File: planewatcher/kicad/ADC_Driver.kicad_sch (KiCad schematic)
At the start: 25 parts, among them U10 AD8138ARZ, U3 OPA2320

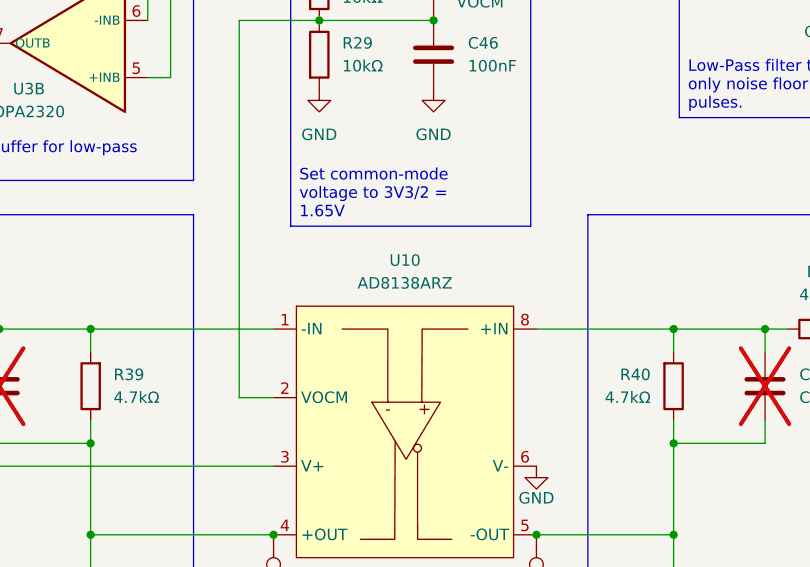
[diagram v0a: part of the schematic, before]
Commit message: Replace TADJ prototype trimmer with voltage divider
Voltage divider sets the ADL5513 TADJ pin to approximately 0.85 V for 1090 MHz operation
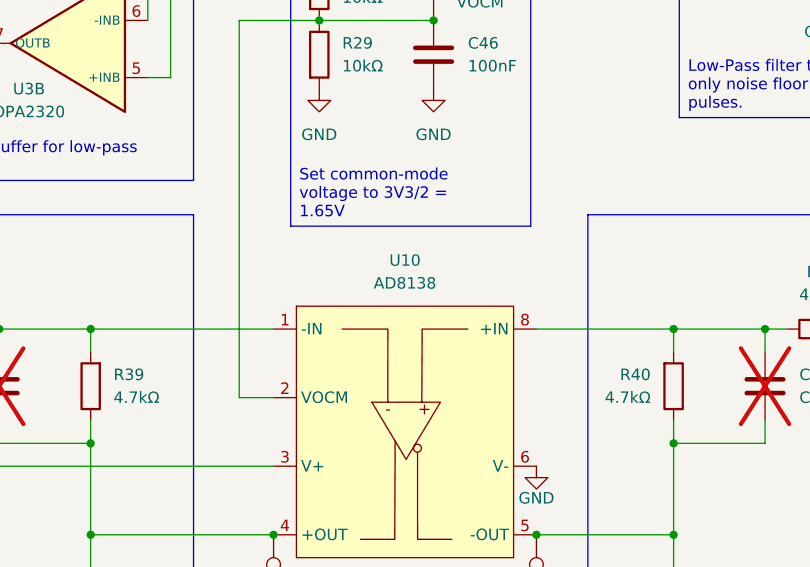
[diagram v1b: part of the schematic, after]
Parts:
- U10: value AD8138ARZ -> AD8138
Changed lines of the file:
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@@
 			)
 		)
-		(property "Value" "AD8138ARZ"
+		(property "Value" "AD8138"
 			(at 147.955 87.63 0)
 			(show_name no)

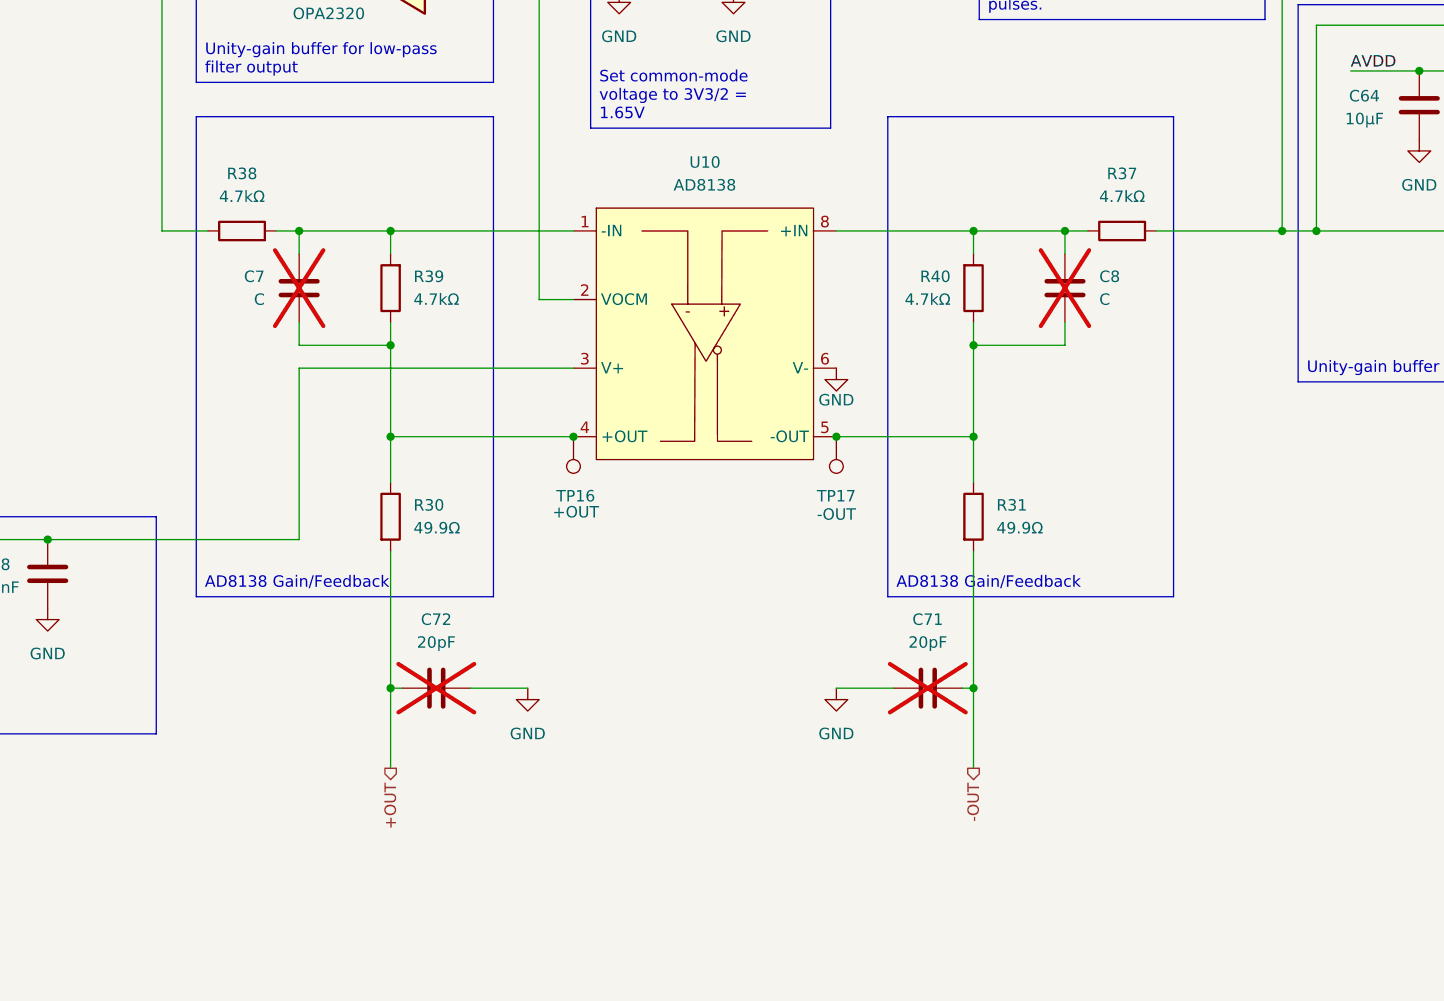
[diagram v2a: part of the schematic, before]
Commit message: Replace AD8138 gain/feedback resistors with resistor array
R37, R38, R39, R40 -> RN1.
Resolves: https://github.com/plane-watch/hardware/pull/5#issuecomment-4815513095
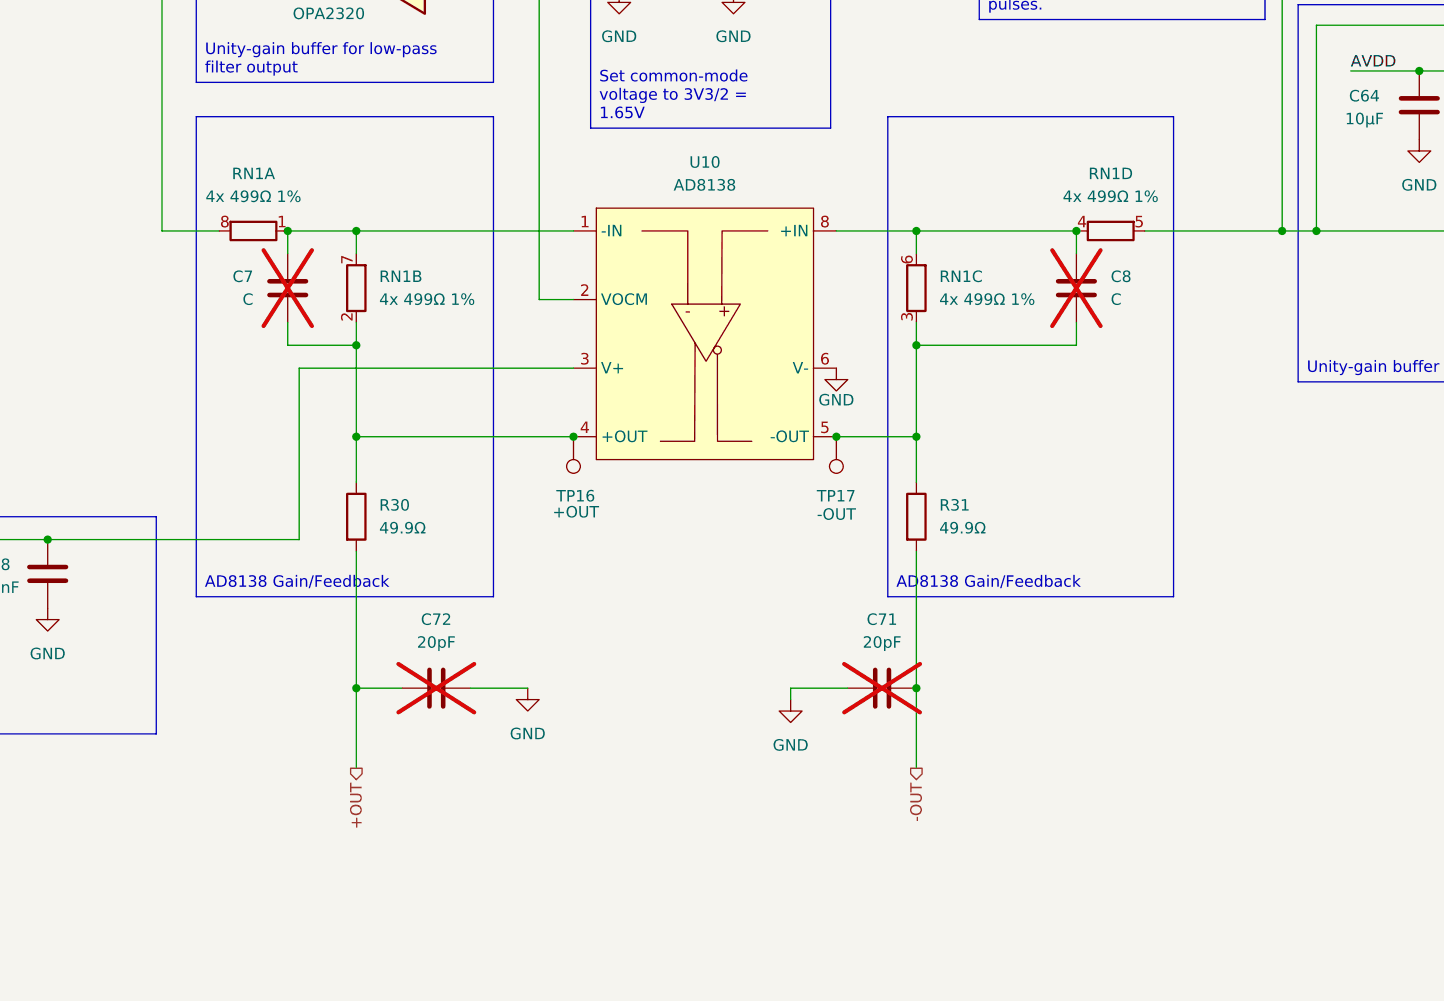
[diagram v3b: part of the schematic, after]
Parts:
- removed R37, R38, R39, R40: 4.7kΩ, Resistor_SMD:R_0402_1005Metric, symbol Device:R
- added RN1: 4x 499Ω 1%, Resistor_SMD:R_Array_Convex_4x0402, symbol Device:R_Pack04_Split
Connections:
- net at C7.2, R30.1, TP16.1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: now also RN1.2 (R2.1)
- net at C8.2, R31.1, TP17.1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: now also RN1.3 (R3.1)
- net at C8.1, U10.8 (+IN): now also RN1.4 (R4.1), RN1.6 (R3.2)
- net at C7.1, U10.1 (-IN): now also RN1.1 (R1.1), RN1.7 (R2.2)
- net at U3.6 (-INB), U3.7 (OUTB): now also RN1.8 (R1.2)
- net at R51.2, U3.1 (OUTA), U3.2 (-INA): now also RN1.5 (R4.2)
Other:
- moved on the sheet: C7, C71, C8, R30, R31

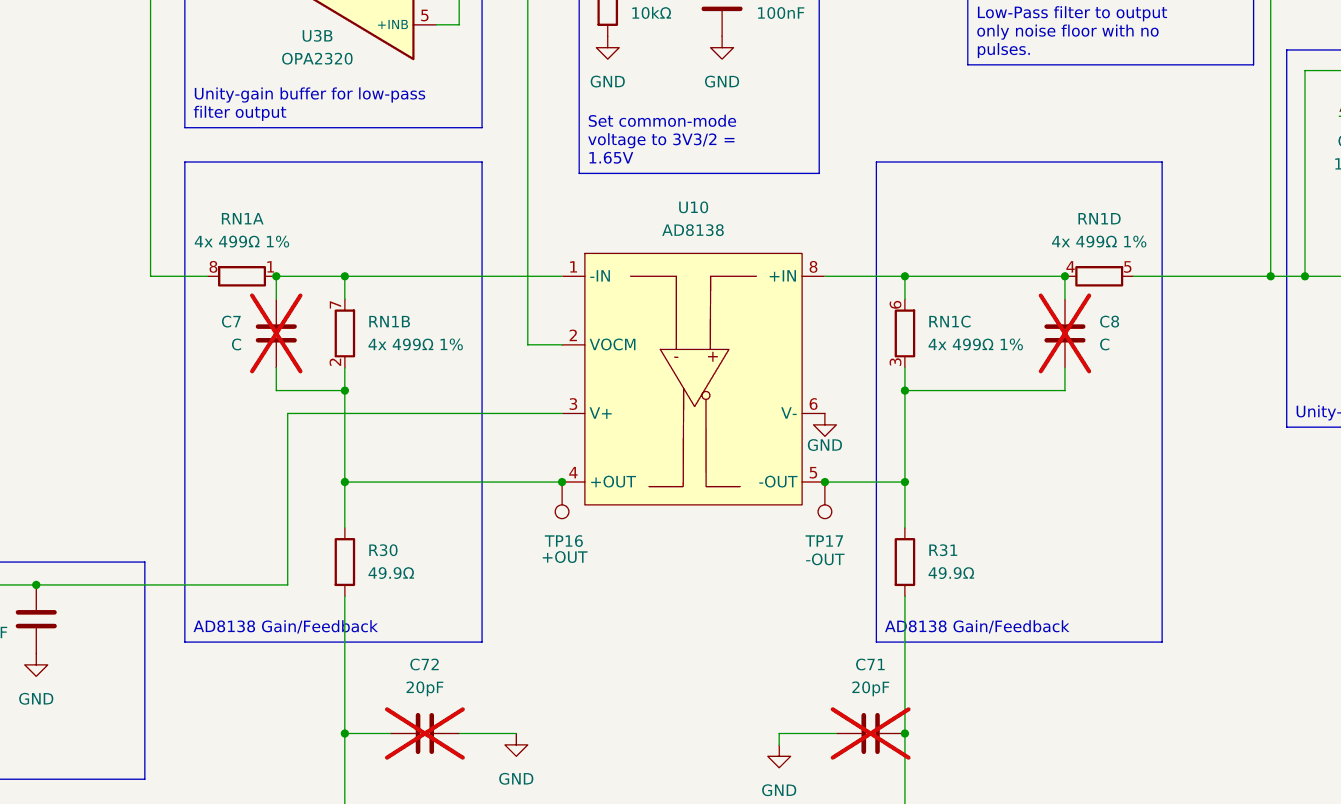
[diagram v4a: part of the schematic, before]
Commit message: Add RF frontend tuning footprints
Add DNP RF tuning footprints around the input match, SAW filter ports, and
log detector input path. Update schematic annotations for VNA-populated C/L/R
matching options, mark AD8138 feedback caps as optional, and update the PCB
layout for the new RF frontend tuning network.
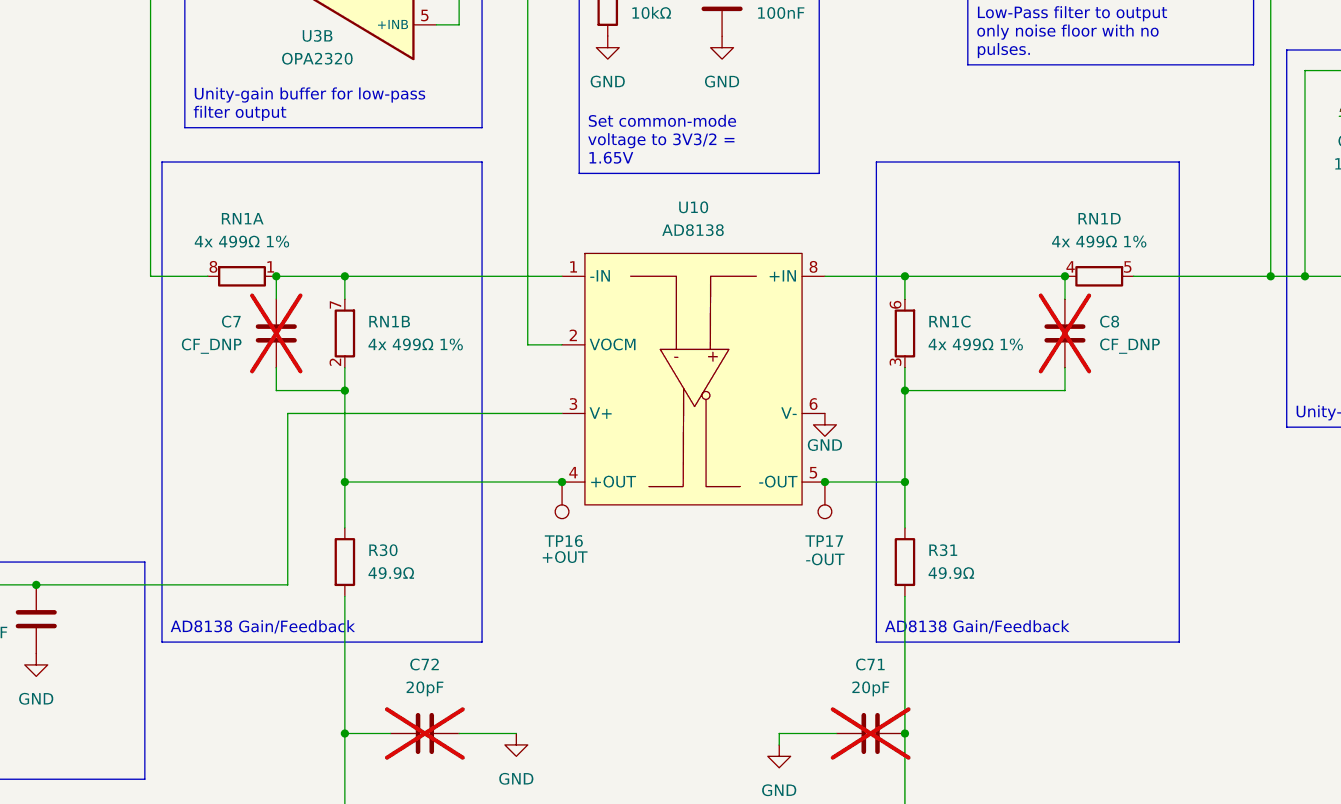
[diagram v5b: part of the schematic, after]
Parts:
- C7: value C -> CF_DNP
- C8: value C -> CF_DNP; Purpose Feedback resistor capacitor, Cf from AD8138 datasheet, figure 42 -> Feedback resistor capacitor, Cf from AD8138 datasheet, figure 42, populate if needed.
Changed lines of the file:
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@@
 	(text_box "AD8138 Gain/Feedback"
 		(exclude_from_sim no)
-		(at 91.44 80.01 0)
-		(size 33.02 53.34)
+		(at 88.9 80.01 0)
+		(size 35.56 53.34)
 		(margins 0.9525 0.9525 0.9525 0.9525)
 		(stroke
@@
 		(exclude_from_sim no)
 		(at 168.275 80.01 0)
-		(size 31.75 53.34)
+		(size 33.655 53.34)
 		(margins 0.9525 0.9525 0.9525 0.9525)
 		(stroke
@@
 			)
 		)
-		(property "Value" "C"
+		(property "Value" "CF_DNP"
 			(at 193.04 100.3299 0)
 			(show_name no)
@@
 			)
 		)
-		(property "Purpose" "Feedback resistor capacitor, Cf from AD8138 datasheet, figure 42"
+		(property "Purpose" "Feedback resistor capacitor, Cf from AD8138 datasheet, figure 42, populate if needed."
 			(at 189.23 99.06 0)
 			(hide yes)
@@
 			)
 		)
-		(property "Value" "C"
+		(property "Value" "CF_DNP"
 			(at 97.79 100.3299 0)
 			(show_name no)

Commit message: Change all test point footprints to TestPoint_THTPad_D1.0mm_Drill0.5mm
Had to move TP15 slightly to prevent it shorting to 3V3.
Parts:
- TP15, TP16, TP17, TP2: footprint TestPoint:TestPoint_Pad_D1.0mm -> TestPoint:TestPoint_THTPad_D1.0mm_Drill0.5mm
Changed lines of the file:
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@@
 			)
 		)
-		(property "Footprint" "TestPoint:TestPoint_Pad_D1.0mm"
+		(property "Footprint" "TestPoint:TestPoint_THTPad_D1.0mm_Drill0.5mm"
 			(at 157.48 115.57 0)
 			(hide yes)
@@
 			)
 		)
-		(property "Footprint" "TestPoint:TestPoint_Pad_D1.0mm"
+		(property "Footprint" "TestPoint:TestPoint_THTPad_D1.0mm_Drill0.5mm"
 			(at 128.27 115.57 0)
 			(hide yes)
@@
 			)
 		)
-		(property "Footprint" "TestPoint:TestPoint_Pad_D1.0mm"
+		(property "Footprint" "TestPoint:TestPoint_THTPad_D1.0mm_Drill0.5mm"
 			(at 185.42 41.91 0)
 			(hide yes)
@@
 			)
 		)
-		(property "Footprint" "TestPoint:TestPoint_Pad_D1.0mm"
+		(property "Footprint" "TestPoint:TestPoint_THTPad_D1.0mm_Drill0.5mm"
 			(at 156.21 58.42 0)
 			(hide yes)

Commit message: Update land pattern for ESD diodes to match mfr datasheet
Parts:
- U3: Purpose Two channel, high-precision, low-noise, RRIO, CMOS operatio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 -> Dual high-precision, low-noise, RRIO CMOS operational ampli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
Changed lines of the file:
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@@
 			)
 		)
-		(property "Purpose" "Two channel, high-precision, low-noise, RRIO, CMOS operational amplifiers with shutdown function"
+		(property "Purpose" "Dual high-precision, low-noise, RRIO CMOS operational amplifier. Non-shutdown OPA2320AIDRGT variant."
 			(at 111.76 45.72 0)
 			(hide yes)
@@
 			)
 		)
-		(property "Purpose" "Two channel, high-precision, low-noise, RRIO, CMOS operational amplifiers with shutdown function"
+		(property "Purpose" "Dual high-precision, low-noise, RRIO CMOS operational amplifier. Non-shutdown OPA2320AIDRGT variant."
 			(at 250.19 77.47 0)
 			(hide yes)

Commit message: Update purpose fields with more descriptive text for future me
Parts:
- C7, C8: Purpose Feedback resistor capacitor, Cf from AD8138 datasheet, figu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 -> Optional DNP AD8138 feedback capacitor (Cf) for bandwidth/s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
- C71, C72: Purpose Optional shunt capacitance for ADC-driver output and anti-a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 -> Shunt capacitor at the AD9203 differential input for ADC in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
- C9: Purpose Shunt capacitor in low-pass filter to output noise floor -> Forms the slow low-pass baseline/noise-floor filter from VL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
- R30, R31: Purpose AD8138 input/output termination and gain-setting resistor f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 -> Series output isolation/termination resistor between AD8138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
- R51: Purpose Series resistor in low-pass filter to output noise floor -> Forms the slow low-pass baseline/noise-floor filter from VL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
- TP2: Purpose (none) -> Provides oscilloscope/DMM probe access to the slow noise-fl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
- U10: Purpose Converts and buffers the detector output into a differentia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 -> Fully differential ADC driver; converts the buffered detect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
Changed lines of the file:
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@@
 			)
 		)
-		(property "Purpose" "AD8138 input/output termination and gain-setting resistor for the differential ADC driver."
+		(property "Purpose" "Series output isolation/termination resistor between AD8138 output and AD9203 input; works with the shunt capacitor to tune ADC input filtering/settling."
 			(at 109.22 124.46 0)
 			(hide yes)
@@
 			)
 		)
-		(property "Purpose" "Feedback resistor capacitor, Cf from AD8138 datasheet, figure 42, populate if needed."
+		(property "Purpose" "Optional DNP AD8138 feedback capacitor (Cf) for bandwidth/stability tuning per datasheet guidance."
 			(at 189.23 99.06 0)
 			(hide yes)
@@
 			)
 		)
-		(property "Purpose" "AD8138 input/output termination and gain-setting resistor for the differential ADC driver."
+		(property "Purpose" "Series output isolation/termination resistor between AD8138 output and AD9203 input; works with the shunt capacitor to tune ADC input filtering/settling."
 			(at 171.45 124.46 0)
 			(hide yes)
@@
 			)
 		)
-		(property "Purpose" "Feedback resistor capacitor, Cf from AD8138 datasheet, figure 42"
+		(property "Purpose" "Optional DNP AD8138 feedback capacitor (Cf) for bandwidth/stability tuning per datasheet guidance."
 			(at 101.6 99.06 0)
 			(hide yes)
@@
 			)
 		)
-		(property "Purpose" "Converts and buffers the detector output into a differential signal for the ADC."
+		(property "Purpose" "Fully differential ADC driver; converts the buffered detector signal relative to the slow baseline into a differential signal centered at VOCM for U11."
 			(at 147.32 87.63 0)
 			(hide yes)
@@
 			)
 		)
+		(property "Purpose" "Provides oscilloscope/DMM probe access to the slow noise-floor/baseline node."
+			(at 180.34 41.91 0)
+			(hide yes)
+			(show_name no)
+			(do_not_autoplace no)
+			(effects
+				(font
+					(size 1.27 1.27)
+				)
+			)
+		)
 		(property "Sim.Device" ""
 			(at 180.34 41.91 0)
@@
 			)
 		)
-		(property "Purpose" "Shunt capacitor in low-pass filter to output noise floor"
+		(property "Purpose" "Forms the slow low-pass baseline/noise-floor filter from VLOG_IN before buffering by U3B."
 			(at 194.31 50.8 0)
 			(hide yes)
@@
 			)
 		)
-		(property "Purpose" "Optional shunt capacitance for ADC-driver output and anti-alias response tuning."
+		(property "Purpose" "Shunt capacitor at the AD9203 differential input for ADC input filtering, settling, and anti-alias response tuning."
 			(at 167.64 143.51 0)
 			(hide yes)
@@
 			)
 		)
-		(property "Purpose" "Series resistor in low-pass filter to output noise floor"
+		(property "Purpose" "Forms the slow low-pass baseline/noise-floor filter from VLOG_IN before buffering by U3B."
 			(at 203.2 41.91 90)
 			(hide yes)
@@
 			)
 		)
-		(property "Purpose" "Optional shunt capacitance for ADC-driver output and anti-alias response tuning."
+		(property "Purpose" "Shunt capacitor at the AD9203 differential input for ADC input filtering, settling, and anti-alias response tuning."
 			(at 118.11 143.51 0)
 			(hide yes)
